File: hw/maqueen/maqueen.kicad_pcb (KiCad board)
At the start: 2 copper layers, 7 parts, among them IC1 MSP430FR2355TPT, J1 conn_DFrobot

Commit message: constraints + crystal
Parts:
- added C1: 10u, Capacitor_SMD:C_0805_2012Metric, F.Cu at (179.2, 57.6)
- added C2: 100n, Capacitor_SMD:C_0805_2012Metric, F.Cu at (179.2, 60.6)
- added C3: 100n, Capacitor_SMD:C_0805_2012Metric, F.Cu at (179.2, 63.6)
- added C4: 10u, Capacitor_SMD:C_0805_2012Metric, F.Cu at (183.7, 57.6)
- added C5: 100n, Capacitor_SMD:C_0805_2012Metric, F.Cu at (183.7, 60.6)
- added C6: 10u, Capacitor_SMD:C_0805_2012Metric, F.Cu at (183.7, 63.6)
- added C7: 100n, Capacitor_SMD:C_0805_2012Metric, F.Cu at (188.1, 57.6)
- added C8: 10u, Capacitor_SMD:C_0805_2012Metric, F.Cu at (188.1, 60.6)
- added C9: 2.2n, Capacitor_SMD:C_0805_2012Metric, F.Cu at (188.1, 63.6)
- added Cload1: 12.5n, Capacitor_SMD:C_0805_2012Metric, F.Cu at (237.9, 60.1)
- added Cload2: 12.5n, Capacitor_SMD:C_0805_2012Metric, F.Cu at (237.9, 63.1)
- added J2: ESP01, Connector_PinHeader_2.54mm:PinHeader_2x04_P2.54mm_Vertical, F.Cu at (205.9, 58.4)
- added J3: SBW, Connector_PinHeader_2.54mm:PinHeader_1x03_P2.54mm_Vertical, F.Cu at (232.1, 58.4)
- added LCD1: LCD_2x16_I2C, MiSE:LCD_2x16_I2C(Midas), F.Cu at (210.5, 41.5)
- added R10: 10k, Resistor_SMD:R_0805_2012Metric, F.Cu at (201.4, 60.5)
- added R11: 47k, Resistor_SMD:R_0805_2012Metric, F.Cu at (201.4, 63.4)
- added R2: 2.2k, Resistor_SMD:R_0805_2012Metric, F.Cu at (192.5, 57.5)
- added R3: 2.2k, Resistor_SMD:R_0805_2012Metric, F.Cu at (192.5, 60.5)
- added R5: 10k, Resistor_SMD:R_0805_2012Metric, F.Cu at (192.5, 63.4)
- added R6: 10k, Resistor_SMD:R_0805_2012Metric, F.Cu at (196.9, 57.5)
- added R7: 10k, Resistor_SMD:R_0805_2012Metric, F.Cu at (196.9, 60.5)
- added R8: 10k, Resistor_SMD:R_0805_2012Metric, F.Cu at (196.9, 63.4)
- added R9: 10k, Resistor_SMD:R_0805_2012Metric, F.Cu at (201.4, 57.5)
- added SW1: RST, Button_Switch_THT:SW_PUSH_6mm, F.Cu at (212.8, 58.1)
- added U1: LMV324, Package_SO:SOIC-14_3.9x8.7mm_P1.27mm, F.Cu at (225.5, 61.2)
- added Y1: Crystal, Connector_PinHeader_1.27mm:PinHeader_1x02_P1.27mm_Vertical, F.Cu at (242.2, 60.3)
- moved IC1 83.4 mm to (229.6, 128.1)
- moved R4 83.4 mm to (230.9, 136.1)
- moved RV2 83.4 mm to (233.6, 115.8)
- moved S1 83.4 mm to (234.4, 91.8)
- moved R1 83.4 mm to (226.2, 136.1)
- moved RV1 83.4 mm to (225.5, 115.8)
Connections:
- IC1 pad 2: unconnected-(IC1-P1.1/UCB0CLK/ACLK/OA0O/COMP0.1/A1-Pad2) -> LR_JOYSTICK
- IC1 pad 3: unconnected-(IC1-P1.0/UCB0STE/SMCLK/COMP0.0/A0/VEREF+-Pad3) -> FB_JOYSTICK
- IC1 pad 37: unconnected-(IC1-P3.5/OA3O-Pad37) -> R_JOYSTICK
- IC1 pad 38: unconnected-(IC1-P3.4/SMCLK-Pad38) -> F_JOYSTICK
- IC1 pad 4: unconnected-(IC1-TEST/SBWTCK-Pad4) -> TCK
- IC1 pad 44: unconnected-(IC1-P3.3/OA2+-Pad44) -> B_JOYSTICK
- IC1 pad 47: unconnected-(IC1-P3.0/MCLK-Pad47) -> L_JOYSTICK
- IC1 pad 5: unconnected-(IC1-~{RST}/NMI/SBWTDIO-Pad5) -> TDO/TDI
- IC1 pad 8: unconnected-(IC1-P2.7/TB0CLK/XIN-Pad8) -> Net-(IC1-P2.7/TB0CLK/XIN)
- IC1 pad 9: unconnected-(IC1-P2.6/MCLK/XOUT-Pad9) -> Net-(IC1-P2.6/MCLK/XOUT)
- S1 pad 12: unconnected-(S1-2'-Pad12) -> FB_JOYSTICK
- S1 pad 2: unconnected-(S1-Pad2) -> LR_JOYSTICK

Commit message: netclasses, specs and more
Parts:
- moved Y1 100.5 mm to (155.3, 110.7)
- moved Cload1 100.5 mm to (151.0, 110.5)
- moved Cload2 100.5 mm to (151.0, 113.5)
- moved LCD1 98.4 mm to (131.1, 99.6), turned to 90 degrees
- moved J2 92.7 mm to (152.6, 134.2), turned to 90 degrees
- moved R4 83.5 mm to (187.0, 65.1)
- moved IC1 83.5 mm to (151.1, 99.9), turned to 90 degrees
- moved SW1 73.9 mm to (163.6, 113.2)
- moved RV2 73.3 mm to (176.0, 70.4), turned to 90 degrees
- moved J3 70.4 mm to (183.0, 108.8)
- moved S1 69.0 mm to (166.0, 83.0), turned to 90 degrees
- moved U1 67.7 mm to (171.0, 101.2)
- moved RV1 52.1 mm to (176.5, 133.8), turned to 90 degrees
- moved J1 46.3 mm to (127.1, 99.9)
- moved R1 39.6 mm to (186.9, 131.9)
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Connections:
- net Net-(IC1-P1.6/UCA0RXD/UCA0SOMI/TB0.1/TDI/TCLK/OA1-/A6) renamed /WIFI_UART_RX
- net Net-(IC1-P1.7/UCA0TXD/UCA0SIMO/TB0.2/TDO/OA1+/A7/VREF+) renamed /WIFI_UART_TX
- net Net-(IC1-P2.6/MCLK/XOUT) renamed /XOUT
- net Net-(IC1-P2.7/TB0CLK/XIN) renamed /XIN
- net Net-(IC1-P5.0/TB2.1/MFM.RX/A8) renamed /PHOTO1
- net Net-(IC1-P5.1/TB2.2/MFM.TX/A9) renamed /PHOTO2
- net Net-(IC1-P5.2/TB2CLK/A10) renamed /RST_LCD
- net Net-(IC1-P6.0/TB3.1) renamed /P6.0
- net Net-(IC1-P6.1/TB3.2) renamed /P6.1
- net Net-(IC1-P6.2/TB3.3) renamed /P6.2
- net Net-(IC1-P6.3/TB3.4) renamed /P6.3
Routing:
- net GND: track 0.00 -> 7.08 mm, vias 0 -> 2
- added copper zone on F.Cu, net +3.3V
- added copper zone on B.Cu, net GND
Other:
- board outline added: 80 x 75 mm

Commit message: te toca, miquel
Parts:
- moved C2 89.0 mm to (150.0, 108.8), turned to -90 degrees
- moved J2 69.1 mm to (159.5, 65.5), turned to -90 degrees
- moved J3 31.6 mm to (163.9, 134.0), turned to 90 degrees
- moved S1 16.4 mm to (182.2, 85.2), turned to -90 degrees
- moved SW1 10.5 mm to (163.8, 123.8)
- moved RV2 6.98 mm to (183.0, 70.0), turned to 180 degrees
- moved Y1 4.94 mm to (151.5, 113.8), turned to 90 degrees
- moved Cload1 4.61 mm to (149.3, 114.8), turned to -90 degrees
- moved RV1 4.26 mm to (178.0, 129.8), turned to 0 degrees
- moved Cload2 4.11 mm to (154.9, 114.8), turned to -90 degrees
- moved R4 2.37 mm to (187.0, 67.5), turned to 180 degrees
- moved U1 2.13 mm to (172.8, 100.0)
- moved R1 0.35 mm to (187.0, 132.2)
- moved LCD1 0.06 mm to (131.2, 99.6)
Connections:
- net /XIN renamed /CLK+
- net /XOUT renamed /CLK-
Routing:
- net /PHOTO1: track 0.00 -> 85.8 mm
- net B_JOYSTICK: track 0.00 -> 61.1 mm, vias 0 -> 2
- net TDO/TDI: track 0.00 -> 47.6 mm, vias 0 -> 1
- net TCK: track 0.00 -> 47.5 mm, vias 0 -> 1
- net L_JOYSTICK: track 0.00 -> 44.0 mm, vias 0 -> 2
- net R_JOYSTICK: track 0.00 -> 30.0 mm, vias 0 -> 2
- net SDA_I2C: track 0.00 -> 27.2 mm, vias 0 -> 1
- net SCL_I2C: track 0.00 -> 26.0 mm, vias 0 -> 1
- net FB_JOYSTICK: track 0.00 -> 14.2 mm
- net /CLK-: track 0.00 -> 11.7 mm
- net /CLK+: track 0.00 -> 11.7 mm
- net GND: track 7.08 -> 14.1 mm, vias 2 -> 18
- net /PHOTO2: track 0.00 -> 6.52 mm
- net +3.3V: track 0.00 -> 1.81 mm
- added copper zone on F.Cu, net GND

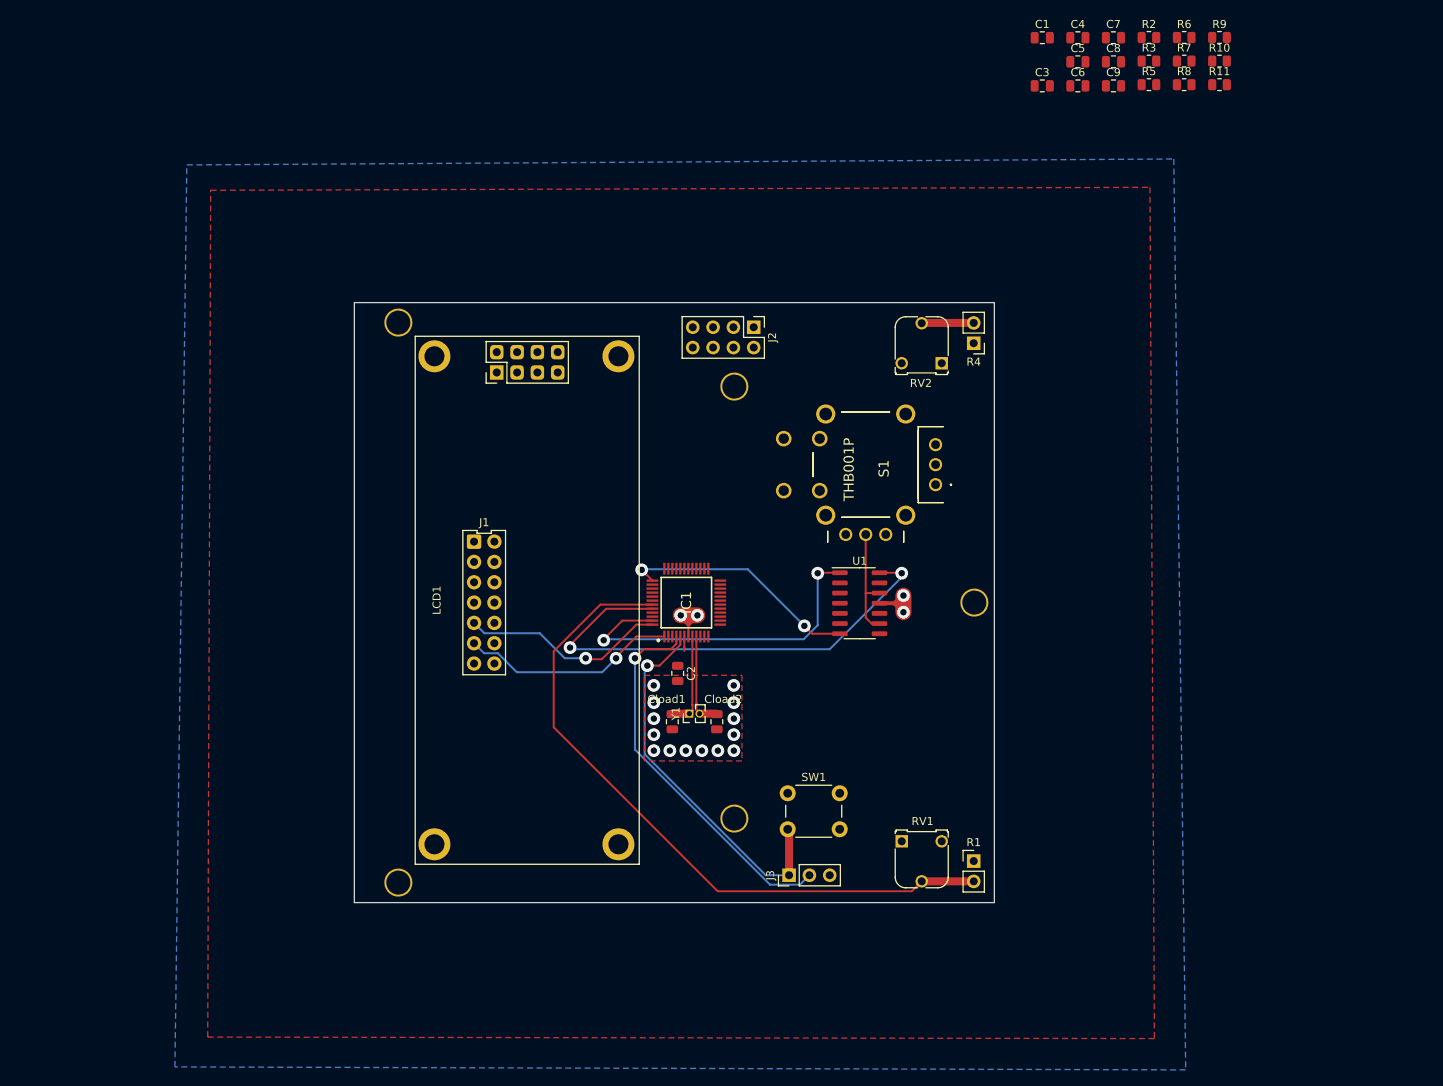
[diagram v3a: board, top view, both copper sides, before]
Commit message: P6.0-P6.3 intercanviats, joystick i LDRs reordenats. Layout no passa DRC per amplada de THs
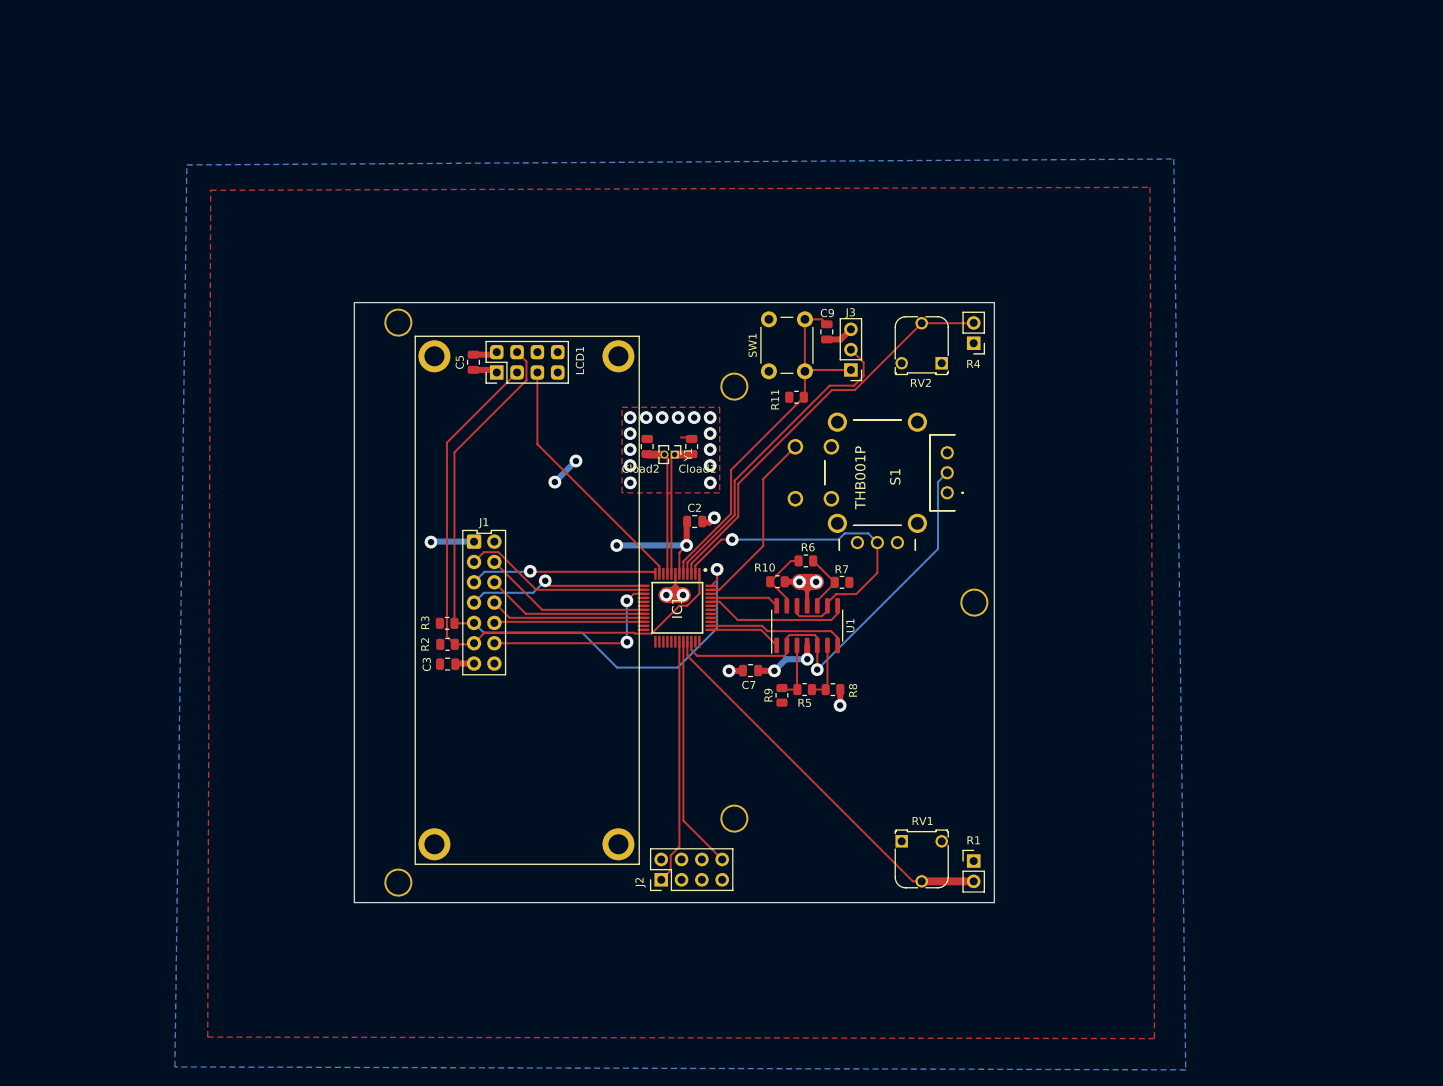
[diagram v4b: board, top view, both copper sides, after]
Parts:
- removed C1, C4, C6, C8: 10u, Capacitor_SMD:C_0805_2012Metric
- moved R2 115.9 mm to (121.2, 105.1)
- moved R3 112.4 mm to (121.2, 102.5)
- moved C3 103.7 mm to (121.2, 107.6)
- moved R9 98.8 mm to (163.0, 111.5), turned to 90 degrees
- moved C7 91.2 mm to (159.1, 108.4), turned to 180 degrees
- moved R8 87.4 mm to (169.4, 110.8)
- moved R5 87.0 mm to (165.9, 110.8)
- moved R10 85.4 mm to (162.5, 97.3)
- moved C5 84.4 mm to (124.5, 69.9), turned to 90 degrees
- moved R6 80.7 mm to (166.0, 94.7), turned to 180 degrees
- moved R7 77.9 mm to (170.5, 97.4), turned to 180 degrees
- moved J2 70.0 mm to (147.9, 134.6), turned to 90 degrees
- moved R11 65.7 mm to (164.8, 74.2)
- moved J3 63.6 mm to (171.7, 70.8), turned to 180 degrees
- moved SW1 52.8 mm to (161.4, 71.0), turned to 90 degrees
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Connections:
- IC1 pad 11: unconnected-(IC1-P2.4/COMP1.1-Pad11) -> RST_LCD
- IC1 pad 2: LR_JOYSTICK -> FB_JOYSTICK
- IC1 pad 3: FB_JOYSTICK -> PHOTO2
- IC1 pad 33: unconnected-(IC1-P1.5/UCA0CLK/TMS/OA1O/A5-Pad33) -> PHOTO1
- IC1 pad 34: unconnected-(IC1-P1.4/UCA0STE/TCK/A4-Pad34) -> LR_JOYSTICK
- IC1 pad 37: R_JOYSTICK -> L_JOYSTICK
- IC1 pad 38: F_JOYSTICK -> R_JOYSTICK
- IC1 pad 41: /RST_LCD -> unconnected-(IC1-P5.2/TB2CLK/A10-Pad41)
- IC1 pad 42: /PHOTO2 -> unconnected-(IC1-P5.1/TB2.2/MFM.TX/A9-Pad42)
- IC1 pad 43: /PHOTO1 -> unconnected-(IC1-P5.0/TB2.1/MFM.RX/A8-Pad43)
- IC1 pad 44: B_JOYSTICK -> F_JOYSTICK
- IC1 pad 45: SEL_JOYSTICK -> B_JOYSTICK
- IC1 pad 47: L_JOYSTICK -> SEL_JOYSTICK
- J1 pad 10: /P6.3 -> /P6.0
- J1 pad 12: DSS_SPI -> SS_SPI
- J1 pad 4: /P6.0 -> /P6.3
- J1 pad 6: /P6.1 -> /P6.2
- J1 pad 8: /P6.2 -> /P6.1
- LCD1 pad 5: /RST_LCD -> RST_LCD
- R1 pad 2: /PHOTO1 -> PHOTO1
- R4 pad 2: /PHOTO2 -> PHOTO2
- RV1 pad 2: /PHOTO1 -> PHOTO1
- RV2 pad 2: /PHOTO2 -> PHOTO2
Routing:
- net /PHOTO1: track 85.8 -> 0.00 mm
- net SCL_I2C: track 26.0 -> 85.0 mm
- net LR_JOYSTICK: track 0.00 -> 54.8 mm, vias 0 -> 1
- net B_JOYSTICK: track 61.1 -> 8.59 mm, vias 2 -> 0
- net PHOTO2: track 0.00 -> 51.4 mm
- net PHOTO1: track 0.00 -> 49.2 mm
- net SDA_I2C: track 27.2 -> 73.8 mm, vias 1 -> 0
- net L_JOYSTICK: track 44.0 -> 8.98 mm, vias 2 -> 0
- net +3.3V: track 1.81 -> 36.3 mm, vias 0 -> 7
- net RST_LCD: track 0.00 -> 31.5 mm
- net /WIFI_UART_TX: track 0.00 -> 30.7 mm
- net FB_JOYSTICK: track 14.2 -> 43.7 mm, vias 0 -> 1
- net /WIFI_UART_RX: track 0.00 -> 29.2 mm
- net SS_SPI: track 0.00 -> 24.3 mm, vias 0 -> 2
- net SCLK_SPI: track 0.00 -> 23.6 mm
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
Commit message: testing points & minor adjustements
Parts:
- moved R9 0.19 mm to (163.0, 111.7)
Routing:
- net +3.3V: track 36.3 -> 41.4 mm
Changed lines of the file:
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@@
   )
   (footprint "Resistor_SMD:R_0805_2012Metric" (layer "F.Cu")
-    (at 163.0275 111.51 90)
+    (at 163.0275 111.7 90)
     (descr "Resistor SMD 0805 (2012 Metric), square (rectangular) end terminal, IPC_7351 nominal, (Body size source: IPC-SM-782 page 72, https://www.pcb-3d.com/wordpress/wp-content/uploads/ipc-sm-782a_amendment_1_and_2.pdf), generated with kicad-footprint-generator")
     (tags "resistor")
@@
   (segment (start 144.5495 103.685) (end 144.6595 103.795) (width 0.25) (layer "F.Cu") (net 1))
   (segment (start 144.6595 103.795) (end 146.735 103.795) (width 0.25) (layer "F.Cu") (net 1))
+  (segment (start 120.3175 107.5825) (end 120.29 107.61) (width 0.75) (layer "F.Cu") (net 2))
   (segment (start 162.09 108.45) (end 160.08 108.45) (width 0.75) (layer "F.Cu") (net 2))
   (segment (start 160.11 108.45) (end 160.07 108.49) (width 0.75) (layer "F.Cu") (net 2))
+  (segment (start 120.3175 105.14) (end 120.3175 107.5825) (width 0.75) (layer "F.Cu") (net 2))
   (segment (start 160.08 108.45) (end 160.05 108.42) (width 0.75) (layer "F.Cu") (net 2))
   (segment (start 166.18 106.98) (end 166.2 107) (width 0.75) (layer "F.Cu") (net 2))
@@
   (segment (start 151.12 89.96) (end 151.07 89.91) (width 0.75) (layer "F.Cu") (net 2))
   (segment (start 151.114504 92.774504) (end 150.21 93.679008) (width 0.25) (layer "F.Cu") (net 2))
+  (segment (start 120.2675 105.09) (end 120.3175 105.14) (width 0.75) (layer "F.Cu") (net 2))
   (segment (start 150.21 93.679008) (end 150.21 96.332) (width 0.25) (layer "F.Cu") (net 2))
   (segment (start 127.055 70.83) (end 127.38 71.155) (width 0.75) (layer "F.Cu") (net 2))
+  (segment (start 120.2675 102.51) (end 120.2675 105.09) (width 0.75) (layer "F.Cu") (net 2))
   (segment (start 124.47 70.83) (end 127.055 70.83) (width 0.75) (layer "F.Cu") (net 2))
   (via (at 137.28 82.22) (size 1.6) (drill 0.8) (layers "F.Cu" "B.Cu") (free) (net 2))
@@
   (segment (start 160.415 103.32) (end 154.198 103.32) (width 0.25) (layer "F.Cu") (net 25))
   (segment (start 164.91 110.745) (end 164.955 110.79) (width 0.25) (layer "F.Cu") (net 33))
-  (segment (start 164.955 110.79) (end 163.22 110.79) (width 0.25) (layer "F.Cu") (net 33))
+  (segment (start 164.955 110.79) (end 163.22 110.79) (width 1) (layer "F.Cu") (net 33))
   (segment (start 164.9775 105.3425) (end 164.91 105.275) (width 0.25) (layer "F.Cu") (net 33))
   (segment (start 163.22 110.79) (end 163.0275 110.5975) (width 0.25) (layer "F.Cu") (net 33))
@@
   (segment (start 168.485 110.79) (end 168.495 110.8) (width 0.25) (layer "F.Cu") (net 34))
   (segment (start 168.5175 105.4775) (end 168.72 105.275) (width 0.25) (layer "F.Cu") (net 34))
-  (segment (start 166.78 110.79) (end 168.485 110.79) (width 0.25) (layer "F.Cu") (net 34))
+  (segment (start 166.78 110.79) (end 168.485 110.79) (width 1) (layer "F.Cu") (net 34))
   (segment (start 169.6275 97.4925) (end 169.6275 97.39) (width 0.25) (layer "F.Cu") (net 35))
   (segment (start 167.45 99.67) (end 169.6275 97.4925) (width 0.25) (layer "F.Cu") (net 35))
